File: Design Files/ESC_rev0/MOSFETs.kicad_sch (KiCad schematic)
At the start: 0 parts

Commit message: update 6
gate driver completion and mosfet init
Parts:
- added Q1: HSBA15810C, footprint:PQFN-8_L6.0-W5.0-P1.27-LS6.0-BL, symbol HSBA15810C:HSBA15810C
- added R12: 4R7, symbol Device:R
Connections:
- new net: Q1.4 (G), R12.2
- new net: Q1.5 (D), Q1.6 (D), Q1.7 (D), Q1.8 (D), Q1.9 (D)
- new net M_H1: R12.1
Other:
- note added: "${TITLE}"
- note added: "Q_CONTROL"
- note added: "Q_SOURCES"
- title: (none) -> MOSFETs

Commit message: update 7
mosfet page completion
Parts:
- added C40, C41: 2n2, symbol Device:C
- added J3, J5, J6: WP-BUTR, WP-BUTR_foot:7461084, symbol Connector_Generic:Conn_01x01
- added NT1, NT2, NT3, NT4, NT5, NT6, NT7, NT8: NetTie_2, symbol Device:NetTie_2
- added Q2, Q3, Q4, Q5, Q6: HSBA15810C, footprint:PQFN-8_L6.0-W5.0-P1.27-LS6.0-BL, symbol HSBA15810C:HSBA15810C
- added R13, R29, R30, R35, R36: 4R7, symbol Device:R
- added R25, R31, R37: 39k, symbol Device:R
- added R26, R33: 0R001_Shunt, symbol Device:R_Shunt
- added R27, R28, R32, R34: 100R, symbol Device:R
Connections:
- net +VDC: now also Q1.5 (D), Q1.6 (D), Q1.7 (D), Q1.8 (D), Q1.9 (D), Q3.5 (D), Q3.6 (D), Q3.7 (D), Q3.8 (D), Q3.9 (D), Q5.5 (D), Q5.6 (D), Q5.7 (D), Q5.8 (D), Q5.9 (D)
- net M_H2: now also R29.1
- net M_H3: now also R35.1
- net M_L1: now also R13.1
- net M_L2: now also R30.1
- net M_L3: now also R36.1
- net PHASE_1: now reaches Q1.1 (S)
- net PHASE_1: now also Q1.2 (S), Q1.3 (S), J3.1 (Pin_1), NT1.2, Q2.5 (D), Q2.6 (D), Q2.7 (D), Q2.8 (D), Q2.9 (D)
- net GH1_RG: now reaches Q1.4 (G), R12.2
- new net: NT3.2, R26.1
- new net: NT2.1, R26.4
- new net: NT5.1, R33.4
- new net: NT6.2, R33.1
- new net GH2_RG: Q3.4 (G), R29.2
- new net GH3_RG: Q5.4 (G), R35.2
- new net GL1_RG: Q2.4 (G), R13.2, R25.1
- new net GL2_RG: Q4.4 (G), R30.2, R31.1
- new net GL3_RG: Q6.4 (G), R36.2, R37.1
- new net GND: NT3.1, NT6.1, NT8.1, R25.2, R31.2, R37.2
- new net PHASE_2: J5.1 (Pin_1), NT4.2, Q3.1 (S), Q3.2 (S), Q3.3 (S), Q4.5 (D), Q4.6 (D), Q4.7 (D), Q4.8 (D), Q4.9 (D)
- new net PHASE_3: J6.1 (Pin_1), NT7.2, Q5.1 (S), Q5.2 (S), Q5.3 (S), Q6.5 (D), Q6.6 (D), Q6.7 (D), Q6.8 (D), Q6.9 (D)
- new net S1_N: R26.2, R28.2
- new net S1_P: R26.3, R27.2
- new net S2_N: R33.2, R34.2
- new net S2_P: R32.2, R33.3
- new net SH1: NT1.1
- new net SH2: NT4.1
- new net SH3: NT7.1
- new net SL1: NT2.2, Q2.1 (S), Q2.2 (S), Q2.3 (S)
- new net SL2: NT5.2, Q4.1 (S), Q4.2 (S), Q4.3 (S)
- new net SL3: NT8.2, Q6.1 (S), Q6.2 (S), Q6.3 (S)
- new net SN1: C40.1, R27.1
- new net SN2: C41.1, R32.1
- new net SP1: C40.2, R28.1
- new net SP2: C41.2, R34.1
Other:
- note added: "OUTPUT PHASE 1"
- note added: "OUTPUT PHASE 2"
- note added: "OUTPUT PHASE 3"
- note added: "PHASE 1"
- note added: "PHASE 2"
- note added: "Place as close as possible to the bulk capacitance"
- note added: "ROUTE AS KEVIN CONNECTIONS"
- note added: "SENSE 1"
- note added: "SENSE 2"
- moved on the sheet: Q1, R12

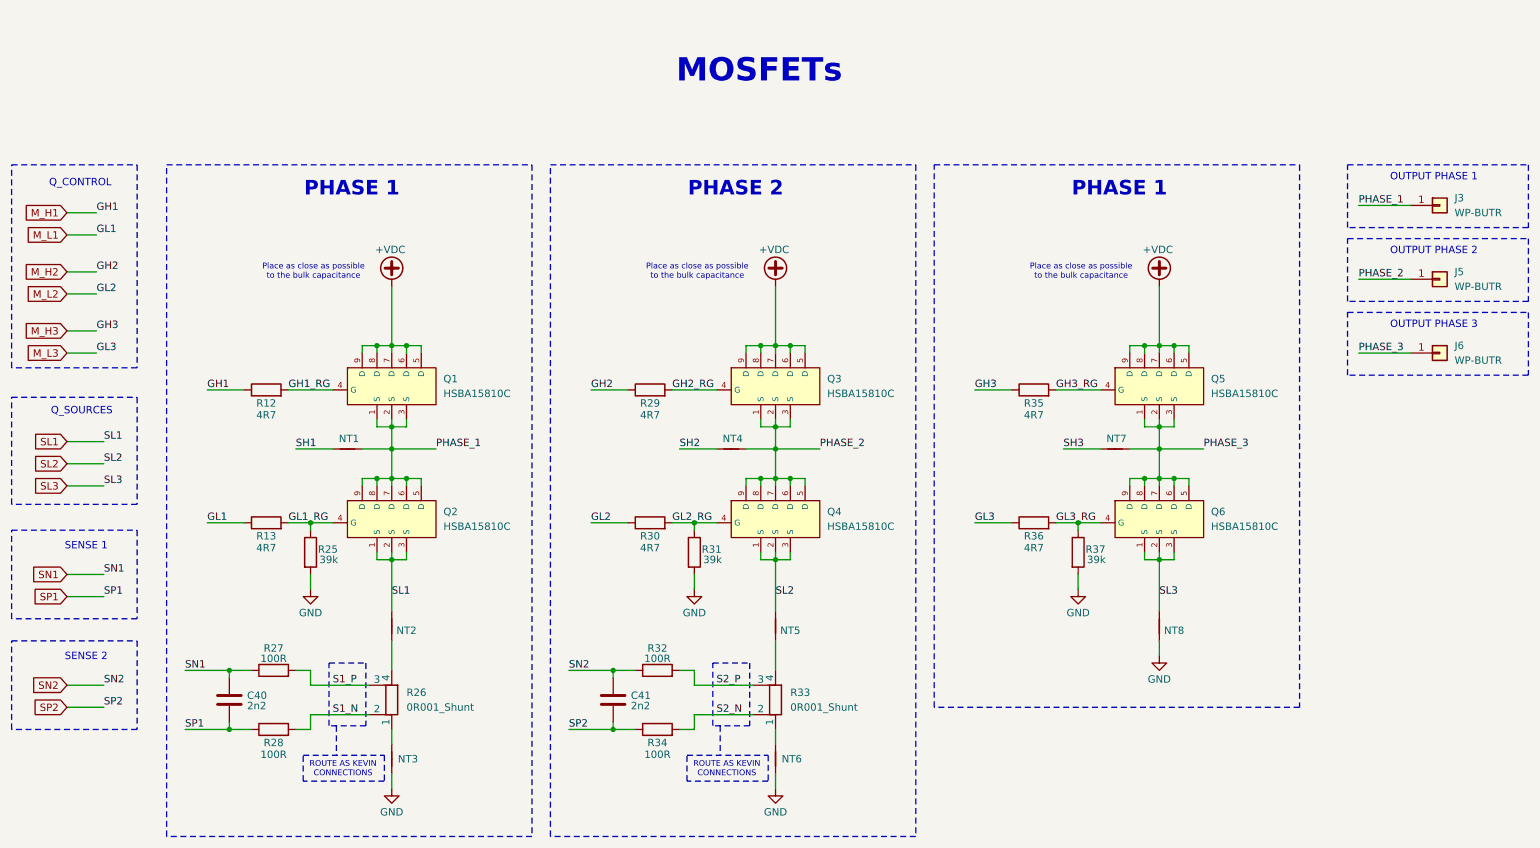
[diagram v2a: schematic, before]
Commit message: UPDATE 12
started schematics revision: edit and added info and circuits to some pages and assigned some footprints for components
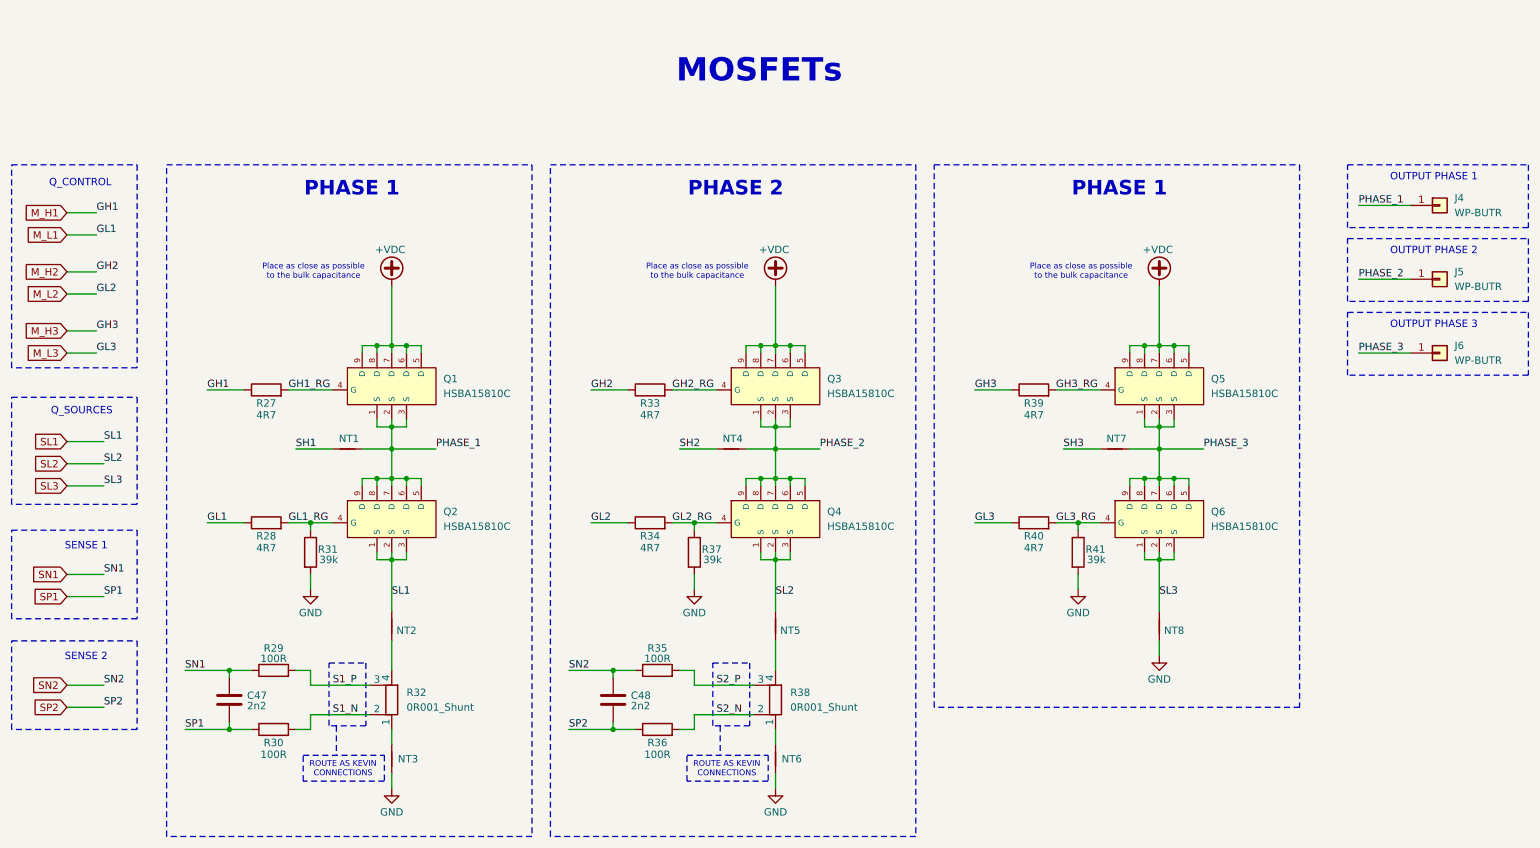
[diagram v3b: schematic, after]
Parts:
- C47: renamed from C40; footprint (none) -> Capacitor_SMD:C_0201_0603Metric
- C48: renamed from C41; footprint (none) -> Capacitor_SMD:C_0201_0603Metric
- renumbered J3 to J4, R12 to R27, R13 to R28, R27 to R29, R28 to R30, R25 to R31, R26 to R32, R29 to R33, R30 to R34, R32 to R35, R34 to R36, R31 to R37, R33 to R38, R35 to R39, R36 to R40, R37 to R41
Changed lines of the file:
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@@
 		(on_board yes)
 		(dnp no)
-		(property "Reference" "#PWR044"
+		(property "Reference" "#PWR054"
 			(at 147.32 66.04 0)
 			(effects
@@
 			(project "ESC_rev0"
 				(path "/7906e740-34c4-4b06-b70f-1daa08872946/b7ae9a45-6f12-4716-8d28-767d1943a1a2"
-					(reference "#PWR044")
+					(reference "#PWR054")
 					(unit 1)
 				)
@@
 		(dnp no)
 		(fields_autoplaced yes)
-		(property "Reference" "R26"
+		(property "Reference" "R32"
 			(at 83.82 133.3499 0)
 			(effects
@@
 			(project ""
 				(path "/7906e740-34c4-4b06-b70f-1daa08872946/b7ae9a45-6f12-4716-8d28-767d1943a1a2"
-					(reference "R26")
+					(reference "R32")
 					(unit 1)
 				)
@@
 		(on_board yes)
 		(dnp no)
-		(property "Reference" "R27"
+		(property "Reference" "R29"
 			(at 60.96 125.73 90)
 			(effects
@@
 			(project "ESC_rev0"
 				(path "/7906e740-34c4-4b06-b70f-1daa08872946/b7ae9a45-6f12-4716-8d28-767d1943a1a2"
-					(reference "R27")
+					(reference "R29")
 					(unit 1)
 				)
@@
 		(on_board yes)
 		(dnp no)
-		(property "Reference" "R30"
+		(property "Reference" "R34"
 			(at 125.73 106.426 90)
 			(effects
@@
 			(project "ESC_rev0"
 				(path "/7906e740-34c4-4b06-b70f-1daa08872946/b7ae9a45-6f12-4716-8d28-767d1943a1a2"
-					(reference "R30")
+					(reference "R34")
 					(unit 1)
 				)
@@
 		(on_board yes)
 		(dnp no)
-		(property "Reference" "#PWR049"
+		(property "Reference" "#PWR058"
 			(at 213.36 133.35 0)
 			(effects
@@
 			(project "ESC_rev0"
 				(path "/7906e740-34c4-4b06-b70f-1daa08872946/b7ae9a45-6f12-4716-8d28-767d1943a1a2"
-					(reference "#PWR049")
+					(reference "#PWR058")
 					(unit 1)
 				)
@@
 		(on_board yes)
 		(dnp no)
-		(property "Reference" "R29"
+		(property "Reference" "R33"
 			(at 125.73 83.566 90)
 			(effects
@@
 			(project "ESC_rev0"
 				(path "/7906e740-34c4-4b06-b70f-1daa08872946/b7ae9a45-6f12-4716-8d28-767d1943a1a2"
-					(reference "R29")
+					(reference "R33")
 					(unit 1)
 				)
@@
 		(on_board yes)
 		(dnp no)
-		(property "Reference" "C41"
+		(property "Reference" "C48"
 			(at 122.428 133.858 0)
 			(effects
@@
 			)
 		)
-		(property "Footprint" ""
+		(property "Footprint" "Capacitor_SMD:C_0201_0603Metric"
 			(at 120.3452 138.43 0)
 			(effects
@@
 			(project "ESC_rev0"
 				(path "/7906e740-34c4-4b06-b70f-1daa08872946/b7ae9a45-6f12-4716-8d28-767d1943a1a2"
-					(reference "C41")
+					(reference "C48")
 					(unit 1)
 				)
@@
 		(on_board yes)
 		(dnp no)
-		(property "Reference" "R37"
+		(property "Reference" "R41"
 			(at 200.66 108.712 0)
 			(effects
@@
 			(project "ESC_rev0"
 				(path "/7906e740-34c4-4b06-b70f-1daa08872946/b7ae9a45-6f12-4716-8d28-767d1943a1a2"
-					(reference "R37")
+					(reference "R41")
 					(unit 1)
 				)
@@
 		(on_board yes)
 		(dnp no)
-		(property "Reference" "R28"
+		(property "Reference" "R30"
 			(at 60.96 141.986 90)
 			(effects
@@
 			(project "ESC_rev0"
 				(path "/7906e740-34c4-4b06-b70f-1daa08872946/b7ae9a45-6f12-4716-8d28-767d1943a1a2"
-					(reference "R28")
+					(reference "R30")
 					(unit 1)
 				)
@@
 		(on_board yes)
 		(dnp no)
-		(property "Reference" "R35"
+		(property "Reference" "R39"
 			(at 191.77 83.566 90)
 			(effects
@@
 			(project "ESC_rev0"
 				(path "/7906e740-34c4-4b06-b70f-1daa08872946/b7ae9a45-6f12-4716-8d28-767d1943a1a2"
-					(reference "R35")
+					(reference "R39")
 					(unit 1)
 				)
@@
 		(dnp no)
 		(fields_autoplaced yes)
-		(property "Reference" "J3"
+		(property "Reference" "J4"
 			(at 264.16 48.2599 0)
 			(effects
@@
 			(project ""
 				(path "/7906e740-34c4-4b06-b70f-1daa08872946/b7ae9a45-6f12-4716-8d28-767d1943a1a2"
-					(reference "J3")
+					(reference "J4")
 					(unit 1)
 				)
@@
 		(on_board yes)
 		(dnp no)
-		(property "Reference" "#PWR047"
+		(property "Reference" "#PWR057"
 			(at 213.36 66.04 0)
 			(effects
@@
 			(project "ESC_rev0"
 				(path "/7906e740-34c4-4b06-b70f-1daa08872946/b7ae9a45-6f12-4716-8d28-767d1943a1a2"
-					(reference "#PWR047")
+					(reference "#PWR057")
 					(unit 1)
 				)
@@
 		(on_board yes)
 		(dnp no)
-		(property "Reference" "R31"
+		(property "Reference" "R37"
 			(at 134.62 108.712 0)
 			(effects
@@
 			(project "ESC_rev0"
 				(path "/7906e740-34c4-4b06-b70f-1daa08872946/b7ae9a45-6f12-4716-8d28-767d1943a1a2"
-					(reference "R31")
+					(reference "R37")
 					(unit 1)
 				)
@@
 		(on_board yes)
 		(dnp no)
-		(property "Reference" "#PWR042"
+		(property "Reference" "#PWR050"
 			(at 67.31 121.92 0)
 			(effects
@@
 			(project ""
 				(path "/7906e740-34c4-4b06-b70f-1daa08872946/b7ae9a45-6f12-4716-8d28-767d1943a1a2"
-					(reference "#PWR042")
+					(reference "#PWR050")
 					(unit 1)
 				)
@@
 		(on_board yes)
 		(dnp no)
-		(property "Reference" "R36"
+		(property "Reference" "R40"
 			(at 191.77 106.426 90)
 			(effects
@@
 			(project "ESC_rev0"
 				(path "/7906e740-34c4-4b06-b70f-1daa08872946/b7ae9a45-6f12-4716-8d28-767d1943a1a2"
-					(reference "R36")
+					(reference "R40")
 					(unit 1)
 				)
@@
 		(on_board yes)
 		(dnp no)
-		(property "Reference" "#PWR043"
+		(property "Reference" "#PWR052"
 			(at 81.28 156.21 0)
 			(effects
@@
 			(project "ESC_rev0"
 				(path "/7906e740-34c4-4b06-b70f-1daa08872946/b7ae9a45-6f12-4716-8d28-767d1943a1a2"
-					(reference "#PWR043")
+					(reference "#PWR052")
 					(unit 1)
 				)
@@
 		(dnp no)
 		(fields_autoplaced yes)
-		(property "Reference" "R33"
+		(property "Reference" "R38"
 			(at 149.86 133.3499 0)
 			(effects
@@
 			(project "ESC_rev0"
 				(path "/7906e740-34c4-4b06-b70f-1daa08872946/b7ae9a45-6f12-4716-8d28-767d1943a1a2"
-					(reference "R33")
+					(reference "R38")
 					(unit 1)
 				)
@@
 		(on_board yes)
 		(dnp no)
-		(property "Reference" "C40"
+		(property "Reference" "C47"
 			(at 56.388 133.858 0)
 			(effects
@@
 			)
 		)
-		(property "Footprint" ""
+		(property "Footprint" "Capacitor_SMD:C_0201_0603Metric"
 			(at 54.3052 138.43 0)
 			(effects
@@
 			(project ""
 				(path "/7906e740-34c4-4b06-b70f-1daa08872946/b7ae9a45-6f12-4716-8d28-767d1943a1a2"
-					(reference "C40")
+					(reference "C47")
 					(unit 1)
 				)
@@
 		(on_board yes)
 		(dnp no)
-		(property "Reference" "R13"
+		(property "Reference" "R28"
 			(at 59.69 106.426 90)
 			(effects
@@
 			(project "ESC_rev0"
 				(path "/7906e740-34c4-4b06-b70f-1daa08872946/b7ae9a45-6f12-4716-8d28-767d1943a1a2"
-					(reference "R13")
+					(reference "R28")
 					(unit 1)
 				)
@@
 		(on_board yes)
 		(dnp no)
-		(property "Reference" "#PWR048"
+		(property "Reference" "#PWR056"
 			(at 199.39 121.92 0)
 			(effects
@@
 			(project "ESC_rev0"
 				(path "/7906e740-34c4-4b06-b70f-1daa08872946/b7ae9a45-6f12-4716-8d28-767d1943a1a2"
-					(reference "#PWR048")
+					(reference "#PWR056")
 					(unit 1)
 				)
@@
 		(on_board yes)
 		(dnp no)
-		(property "Reference" "R34"
+		(property "Reference" "R36"
 			(at 127 141.986 90)
 			(effects
@@
 			(project "ESC_rev0"
 				(path "/7906e740-34c4-4b06-b70f-1daa08872946/b7ae9a45-6f12-4716-8d28-767d1943a1a2"
-					(reference "R34")
+					(reference "R36")
 					(unit 1)
 				)
@@
 		(on_board yes)
 		(dnp no)
-		(property "Reference" "#PWR046"
+		(property "Reference" "#PWR055"
 			(at 147.32 156.21 0)
 			(effects
@@
 			(project "ESC_rev0"
 				(path "/7906e740-34c4-4b06-b70f-1daa08872946/b7ae9a45-6f12-4716-8d28-767d1943a1a2"
-					(reference "#PWR046")
+					(reference "#PWR055")
 					(unit 1)
 				)
@@
 		(on_board yes)
 		(dnp no)
-		(property "Reference" "#PWR041"
+		(property "Reference" "#PWR051"
 			(at 81.28 66.04 0)
 			(effects
@@
 			(project ""
 				(path "/7906e740-34c4-4b06-b70f-1daa08872946/b7ae9a45-6f12-4716-8d28-767d1943a1a2"
-					(reference "#PWR041")
+					(reference "#PWR051")
 					(unit 1)
 				)
@@
 		(on_board yes)
 		(dnp no)
-		(property "Reference" "R12"
+		(property "Reference" "R27"
 			(at 59.69 83.566 90)
 			(effects
@@
 			(project ""
 				(path "/7906e740-34c4-4b06-b70f-1daa08872946/b7ae9a45-6f12-4716-8d28-767d1943a1a2"
-					(reference "R12")
+					(reference "R27")
 					(unit 1)
 				)
@@
 		(on_board yes)
 		(dnp no)
-		(property "Reference" "R25"
+		(property "Reference" "R31"
 			(at 68.58 108.712 0)
 			(effects
@@
 			(project ""
 				(path "/7906e740-34c4-4b06-b70f-1daa08872946/b7ae9a45-6f12-4716-8d28-767d1943a1a2"
-					(reference "R25")
+					(reference "R31")
 					(unit 1)
 				)
@@
 		(on_board yes)
 		(dnp no)
-		(property "Reference" "R32"
+		(property "Reference" "R35"
 			(at 127 125.73 90)
 			(effects
@@
 			(project "ESC_rev0"
 				(path "/7906e740-34c4-4b06-b70f-1daa08872946/b7ae9a45-6f12-4716-8d28-767d1943a1a2"
-					(reference "R32")
+					(reference "R35")
 					(unit 1)
 				)
@@
 		(on_board yes)
 		(dnp no)
-		(property "Reference" "#PWR045"
+		(property "Reference" "#PWR053"
 			(at 133.35 121.92 0)
 			(effects
@@
 			(project "ESC_rev0"
 				(path "/7906e740-34c4-4b06-b70f-1daa08872946/b7ae9a45-6f12-4716-8d28-767d1943a1a2"
-					(reference "#PWR045")
-					(unit 1)
-				)
+					(reference "#PWR053")
+					(unit 1)
+				)
